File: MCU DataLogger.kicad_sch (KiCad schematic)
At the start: 25 parts, among them U1 24LC1025, U2 24LC1025, U3 DS1337S_, U4 ATMEGA328P-AU, Y1 32.768 KH, Y2 16MHz

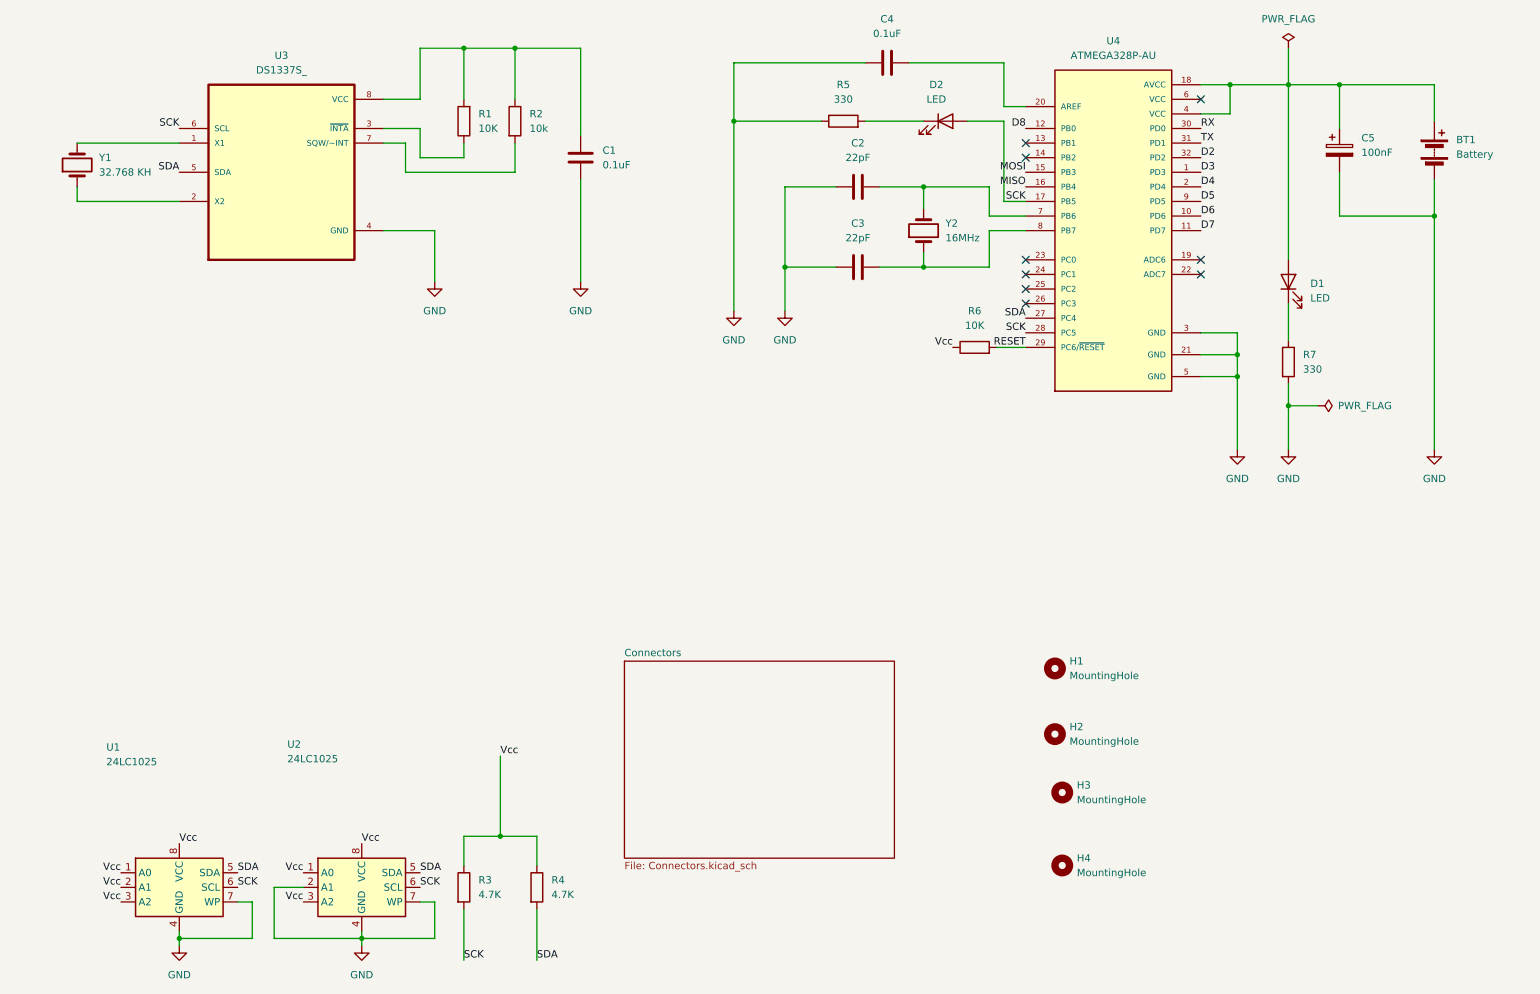
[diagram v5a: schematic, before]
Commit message: Both sheets wired but Vcc in sheet 2 is not connected. Maybe some issue with Kicad mismatch
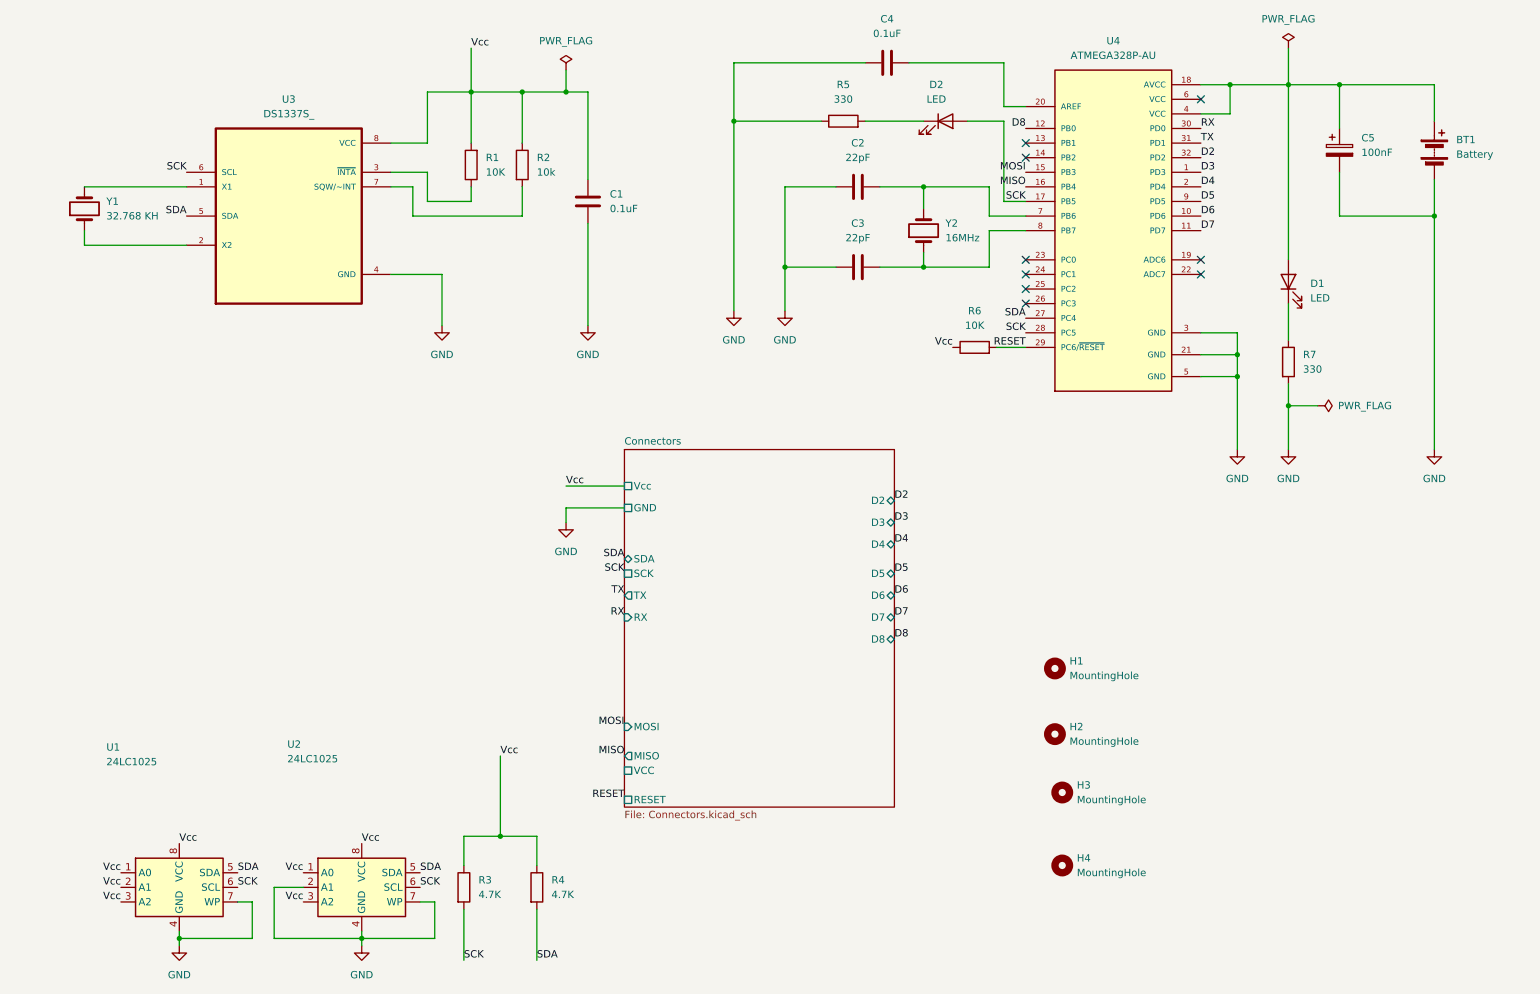
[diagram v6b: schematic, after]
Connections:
- net Vcc: now also C1.2, R1.2, R2.1, U3.8 (VCC)
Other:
- sheet Connectors ports: added D2, D3, D4, D5, D6, D7, D8, GND, MISO, MOSI, RESET, RX, SCK, SDA, TX, VCC, Vcc; removed none
- moved on the sheet: C1, R1, R2, U3, Y1
